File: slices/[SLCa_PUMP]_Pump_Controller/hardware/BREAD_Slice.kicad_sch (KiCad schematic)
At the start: 18 parts, among them J1 Conn_01x10_Female, J2 Term_2, J3 Term_2, J4 Term_2, Q1 TIP120, U1 LM358

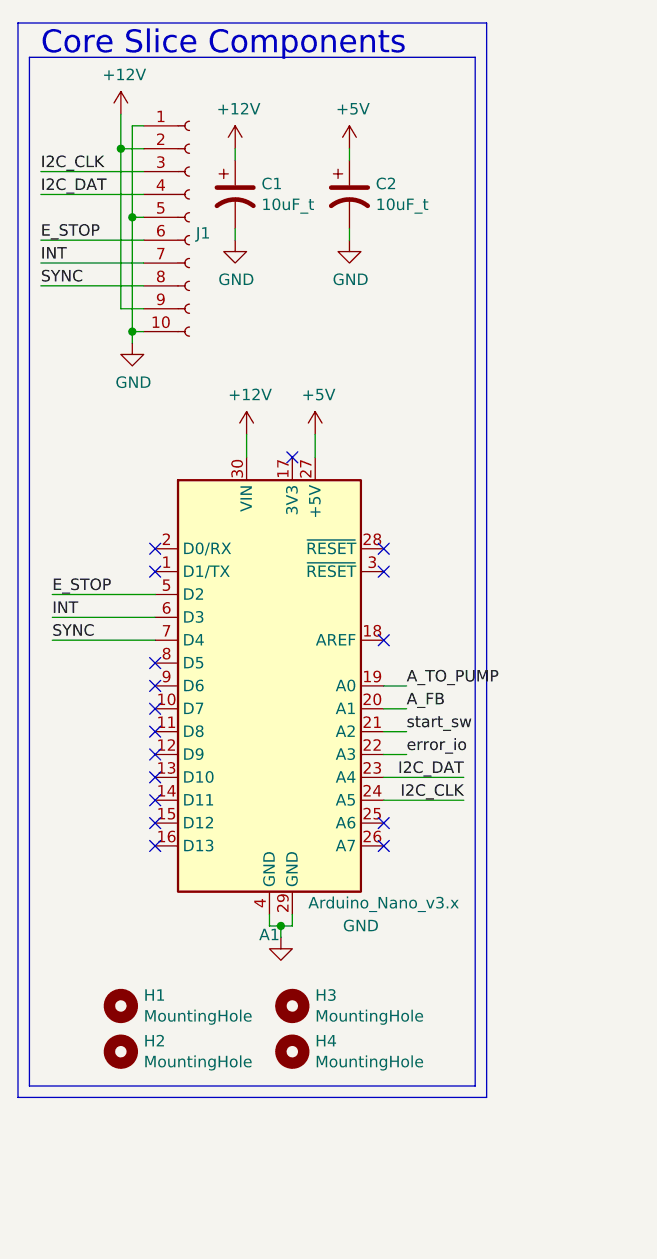
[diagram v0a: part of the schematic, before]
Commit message: restructuring for rpi boards
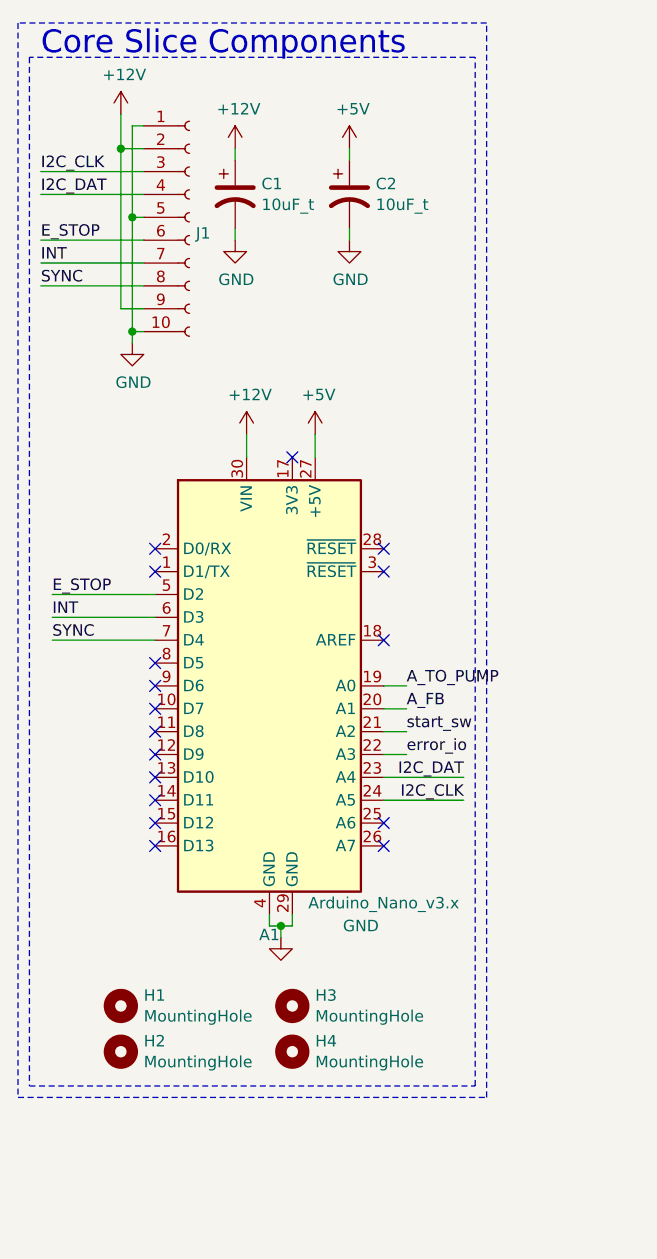
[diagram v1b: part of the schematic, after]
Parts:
- U1: footprint (none) -> OCI:DIP-8_W7.62mm_LongPads
